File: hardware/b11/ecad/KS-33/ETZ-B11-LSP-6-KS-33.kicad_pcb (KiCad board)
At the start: 2 copper layers, 163.9 x 90.2 mm, 339 parts

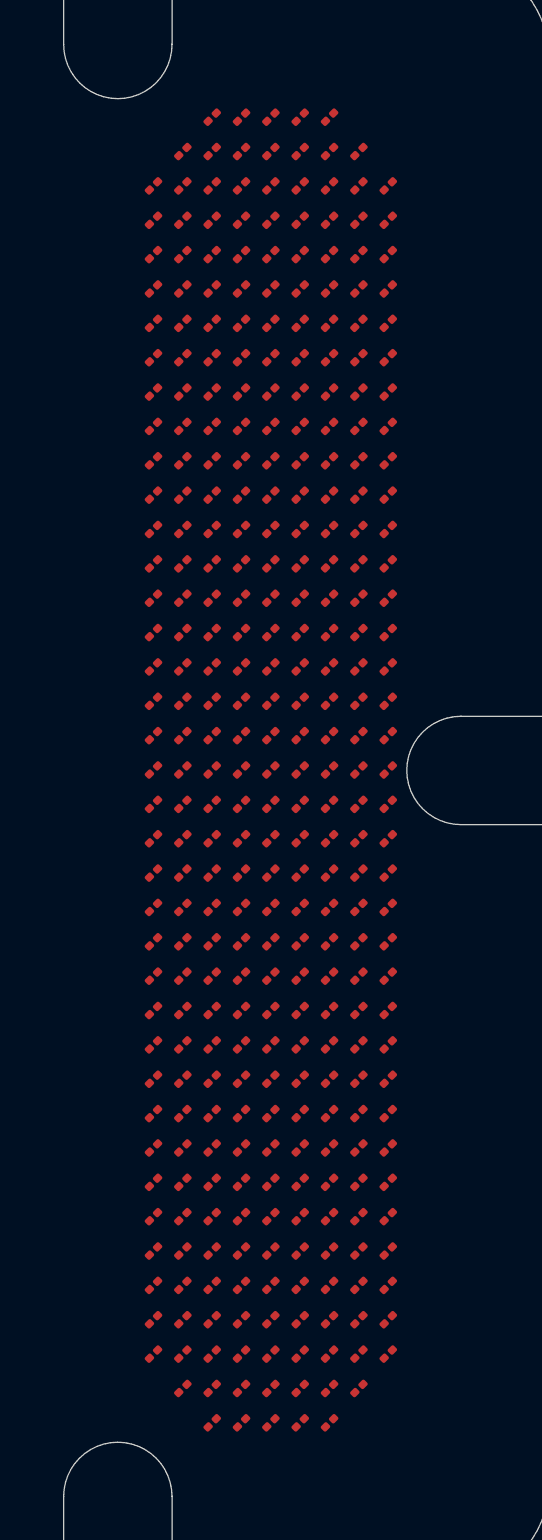
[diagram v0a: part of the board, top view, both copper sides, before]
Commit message: Adjust B11 display LED layout [skip ci]
Signed-off-by: Nikola Secerovski <secersh@gmail.com>
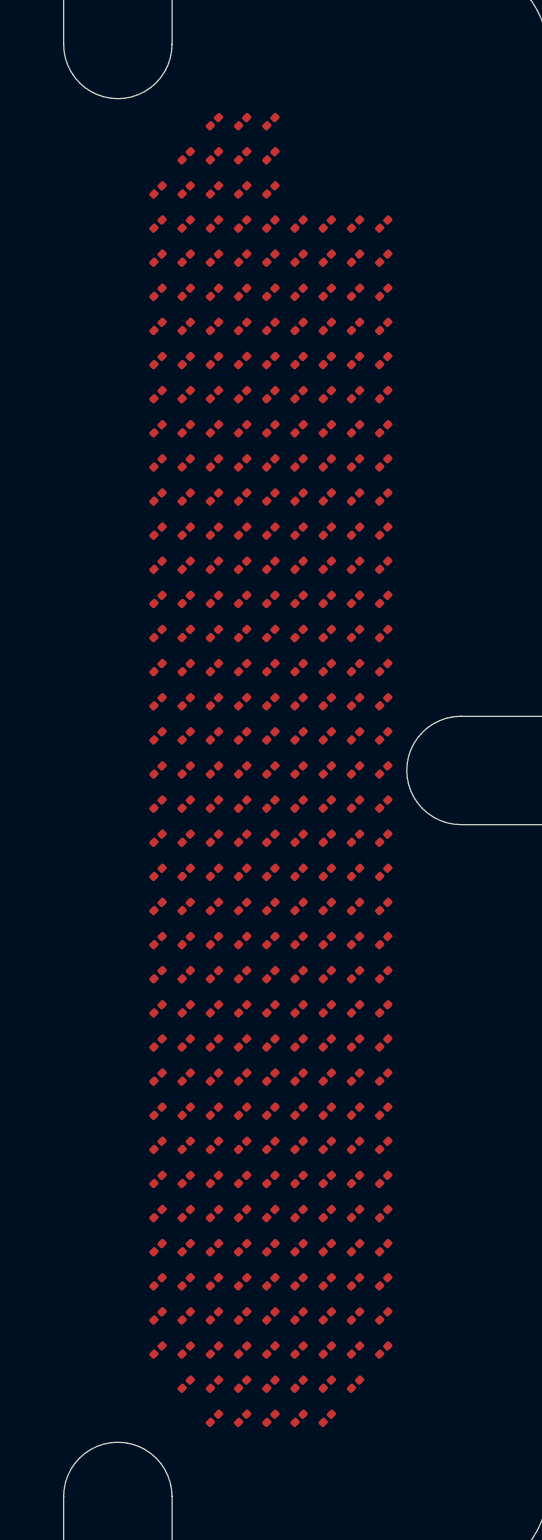
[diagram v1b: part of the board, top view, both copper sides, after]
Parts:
- removed D331, D332, D333, D334, D335, D336, D337, D338, D339: 0201_LED, 0201_LED
- moved D327 8.81 mm to (213.5, 140.2), turned to -135 degrees
- moved D326 8.75 mm to (211.9, 140.2), turned to -135 degrees
- moved D5 6.72 mm to (211.9, 70.3), turned to -135 degrees
- moved D4 6.67 mm to (210.3, 70.3), turned to -135 degrees
- moved D12 5.32 mm to (215.0, 72.2), turned to -135 degrees
- moved D11 5.26 mm to (213.5, 72.2), turned to -135 degrees
- moved D10 5.20 mm to (211.9, 72.2), turned to -135 degrees
- moved D328 5.15 mm to (215.0, 140.2), turned to -135 degrees
- moved D9 5.15 mm to (210.3, 72.2), turned to -135 degrees
- moved D8 5.09 mm to (208.8, 72.2), turned to -135 degrees
- moved D329 5.09 mm to (216.6, 140.2), turned to -135 degrees
- moved D330 5.03 mm to (218.2, 140.2), turned to -135 degrees
- moved D6 3.32 mm to (213.5, 70.3), turned to -135 degrees
- moved D7 3.26 mm to (215.0, 70.3), turned to -135 degrees
- moved D319 2.46 mm to (210.3, 138.3), turned to -135 degrees
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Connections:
- D10 pad 1: LED_CS2 -> LED_CS3
- D10 pad 2: LED_SW6 -> LED_SW3
- D100 pad 1: LED_CS12 -> LED_CS13
- D101 pad 1: LED_CS12 -> LED_CS13
- D102 pad 1: LED_CS12 -> LED_CS13
- D103 pad 1: LED_CS13 -> LED_CS14
- D104 pad 1: LED_CS13 -> LED_CS14
- D105 pad 1: LED_CS13 -> LED_CS14
- D106 pad 1: LED_CS13 -> LED_CS14
- D107 pad 1: LED_CS13 -> LED_CS14
- D108 pad 1: LED_CS13 -> LED_CS14
- D109 pad 1: LED_CS13 -> LED_CS14
- D11 pad 1: LED_CS2 -> LED_CS3
- D11 pad 2: LED_SW7 -> LED_SW4
- D110 pad 1: LED_CS13 -> LED_CS14
- D111 pad 1: LED_CS13 -> LED_CS14
- D112 pad 1: LED_CS14 -> LED_CS15
- D113 pad 1: LED_CS14 -> LED_CS15
- D114 pad 1: LED_CS14 -> LED_CS15
- D115 pad 1: LED_CS14 -> LED_CS15
- D116 pad 1: LED_CS14 -> LED_CS15
- D117 pad 1: LED_CS14 -> LED_CS15
- D118 pad 1: LED_CS14 -> LED_CS15
- D119 pad 1: LED_CS14 -> LED_CS15
- D12 pad 1: LED_CS2 -> LED_CS3
- D12 pad 2: LED_SW8 -> LED_SW5
- D120 pad 1: LED_CS14 -> LED_CS15
- D121 pad 1: LED_CS15 -> LED_CS16
- D122 pad 1: LED_CS15 -> LED_CS16
- D123 pad 1: LED_CS15 -> LED_CS16
- D124 pad 1: LED_CS15 -> LED_CS16
- D125 pad 1: LED_CS15 -> LED_CS16
- D126 pad 1: LED_CS15 -> LED_CS16
- D127 pad 1: LED_CS15 -> LED_CS16
- D128 pad 1: LED_CS15 -> LED_CS16
- D129 pad 1: LED_CS15 -> LED_CS16
- D13 pad 1: LED_CS3 -> LED_CS4
- D130 pad 1: LED_CS16 -> LED_CS17
- D131 pad 1: LED_CS16 -> LED_CS17
- D132 pad 1: LED_CS16 -> LED_CS17
- D133 pad 1: LED_CS16 -> LED_CS17
- D134 pad 1: LED_CS16 -> LED_CS17
- D135 pad 1: LED_CS16 -> LED_CS17
- D136 pad 1: LED_CS16 -> LED_CS17
- D137 pad 1: LED_CS16 -> LED_CS17
- D138 pad 1: LED_CS16 -> LED_CS17
- D139 pad 1: LED_CS17 -> LED_CS18
- D14 pad 1: LED_CS3 -> LED_CS4
- D140 pad 1: LED_CS17 -> LED_CS18
- D141 pad 1: LED_CS17 -> LED_CS18
- D142 pad 1: LED_CS17 -> LED_CS18
- D143 pad 1: LED_CS17 -> LED_CS18
- D144 pad 1: LED_CS17 -> LED_CS18
- D145 pad 1: LED_CS17 -> LED_CS18
- D146 pad 1: LED_CS17 -> LED_CS18
- D147 pad 1: LED_CS17 -> LED_CS18
- D148 pad 1: LED_CS18 -> LED_CS19
- D149 pad 1: LED_CS18 -> LED_CS19
- D15 pad 1: LED_CS3 -> LED_CS4
- D150 pad 1: LED_CS18 -> LED_CS19
- D151 pad 1: LED_CS18 -> LED_CS19
- D152 pad 1: LED_CS18 -> LED_CS19
- D153 pad 1: LED_CS18 -> LED_CS19
- D154 pad 1: LED_CS18 -> LED_CS19
- D155 pad 1: LED_CS18 -> LED_CS19
- D156 pad 1: LED_CS18 -> LED_CS19
- D157 pad 1: LED_CS19 -> LED_CS20
- D158 pad 1: LED_CS19 -> LED_CS20
- D159 pad 1: LED_CS19 -> LED_CS20
- D16 pad 1: LED_CS3 -> LED_CS4
- D160 pad 1: LED_CS19 -> LED_CS20
- D161 pad 1: LED_CS19 -> LED_CS20
- D162 pad 1: LED_CS19 -> LED_CS20
- D163 pad 1: LED_CS19 -> LED_CS20
- D164 pad 1: LED_CS19 -> LED_CS20
- D165 pad 1: LED_CS19 -> LED_CS20
- D166 pad 1: LED_CS20 -> LED_CS21
- D167 pad 1: LED_CS20 -> LED_CS21
- D168 pad 1: LED_CS20 -> LED_CS21
- D169 pad 1: LED_CS20 -> LED_CS21
- D17 pad 1: LED_CS3 -> LED_CS4
- D170 pad 1: LED_CS20 -> LED_CS21
- D171 pad 1: LED_CS20 -> LED_CS21
- D172 pad 1: LED_CS20 -> LED_CS21
- D173 pad 1: LED_CS20 -> LED_CS21
- D174 pad 1: LED_CS20 -> LED_CS21
- D175 pad 1: LED_CS21 -> LED_CS22
- D176 pad 1: LED_CS21 -> LED_CS22
- D177 pad 1: LED_CS21 -> LED_CS22
- D178 pad 1: LED_CS21 -> LED_CS22
- D179 pad 1: LED_CS21 -> LED_CS22
- D18 pad 1: LED_CS3 -> LED_CS4
- D180 pad 1: LED_CS21 -> LED_CS22
- D181 pad 1: LED_CS21 -> LED_CS22
- D182 pad 1: LED_CS21 -> LED_CS22
- D183 pad 1: LED_CS21 -> LED_CS22
- D184 pad 1: LED_CS22 -> LED_CS23
- D185 pad 1: LED_CS22 -> LED_CS23
- D186 pad 1: LED_CS22 -> LED_CS23
- D187 pad 1: LED_CS22 -> LED_CS23
- D188 pad 1: LED_CS22 -> LED_CS23
- D189 pad 1: LED_CS22 -> LED_CS23
- D19 pad 1: LED_CS3 -> LED_CS4
- D190 pad 1: LED_CS22 -> LED_CS23
- D191 pad 1: LED_CS22 -> LED_CS23
- D192 pad 1: LED_CS22 -> LED_CS23
- D193 pad 1: LED_CS23 -> LED_CS24
- D194 pad 1: LED_CS23 -> LED_CS24
- D195 pad 1: LED_CS23 -> LED_CS24
- D196 pad 1: LED_CS23 -> LED_CS24
- D197 pad 1: LED_CS23 -> LED_CS24
- D198 pad 1: LED_CS23 -> LED_CS24
- D199 pad 1: LED_CS23 -> LED_CS24
- D20 pad 1: LED_CS3 -> LED_CS4
- D200 pad 1: LED_CS23 -> LED_CS24
- D201 pad 1: LED_CS23 -> LED_CS24
- D202 pad 1: LED_CS24 -> LED_CS25
- D203 pad 1: LED_CS24 -> LED_CS25
- D204 pad 1: LED_CS24 -> LED_CS25
- D205 pad 1: LED_CS24 -> LED_CS25
- D206 pad 1: LED_CS24 -> LED_CS25
- D207 pad 1: LED_CS24 -> LED_CS25
- D208 pad 1: LED_CS24 -> LED_CS25
- D209 pad 1: LED_CS24 -> LED_CS25
- D21 pad 1: LED_CS3 -> LED_CS4
- D210 pad 1: LED_CS24 -> LED_CS25
- D211 pad 1: LED_CS25 -> LED_CS26
- D212 pad 1: LED_CS25 -> LED_CS26
- D213 pad 1: LED_CS25 -> LED_CS26
- D214 pad 1: LED_CS25 -> LED_CS26
- D215 pad 1: LED_CS25 -> LED_CS26
- D216 pad 1: LED_CS25 -> LED_CS26
- D217 pad 1: LED_CS25 -> LED_CS26
- D218 pad 1: LED_CS25 -> LED_CS26
- D219 pad 1: LED_CS25 -> LED_CS26
- D22 pad 1: LED_CS4 -> LED_CS5
- D220 pad 1: LED_CS26 -> LED_CS27
- D221 pad 1: LED_CS26 -> LED_CS27
- D222 pad 1: LED_CS26 -> LED_CS27
- D223 pad 1: LED_CS26 -> LED_CS27
- D224 pad 1: LED_CS26 -> LED_CS27
- D225 pad 1: LED_CS26 -> LED_CS27
- D226 pad 1: LED_CS26 -> LED_CS27
- D227 pad 1: LED_CS26 -> LED_CS27
- D228 pad 1: LED_CS26 -> LED_CS27
- D229 pad 1: LED_CS27 -> LED_CS28
- D23 pad 1: LED_CS4 -> LED_CS5
- D230 pad 1: LED_CS27 -> LED_CS28
- D231 pad 1: LED_CS27 -> LED_CS28
- D232 pad 1: LED_CS27 -> LED_CS28
- D233 pad 1: LED_CS27 -> LED_CS28
- D234 pad 1: LED_CS27 -> LED_CS28
- D235 pad 1: LED_CS27 -> LED_CS28
- D236 pad 1: LED_CS27 -> LED_CS28
- D237 pad 1: LED_CS27 -> LED_CS28
- D238 pad 1: LED_CS28 -> LED_CS29
- D239 pad 1: LED_CS28 -> LED_CS29
- D24 pad 1: LED_CS4 -> LED_CS5
- D240 pad 1: LED_CS28 -> LED_CS29
- D241 pad 1: LED_CS28 -> LED_CS29
- D242 pad 1: LED_CS28 -> LED_CS29
- D243 pad 1: LED_CS28 -> LED_CS29
- D244 pad 1: LED_CS28 -> LED_CS29
- D245 pad 1: LED_CS28 -> LED_CS29
- D246 pad 1: LED_CS28 -> LED_CS29
- D247 pad 1: LED_CS29 -> LED_CS30
- D248 pad 1: LED_CS29 -> LED_CS30
- D249 pad 1: LED_CS29 -> LED_CS30
- D25 pad 1: LED_CS4 -> LED_CS5
- D250 pad 1: LED_CS29 -> LED_CS30
- D251 pad 1: LED_CS29 -> LED_CS30
- D252 pad 1: LED_CS29 -> LED_CS30
- D253 pad 1: LED_CS29 -> LED_CS30
- D254 pad 1: LED_CS29 -> LED_CS30
- D255 pad 1: LED_CS29 -> LED_CS30
- D256 pad 1: LED_CS30 -> LED_CS31
- D257 pad 1: LED_CS30 -> LED_CS31
- D258 pad 1: LED_CS30 -> LED_CS31
- D259 pad 1: LED_CS30 -> LED_CS31
- D26 pad 1: LED_CS4 -> LED_CS5
- D260 pad 1: LED_CS30 -> LED_CS31
- D261 pad 1: LED_CS30 -> LED_CS31
- D262 pad 1: LED_CS30 -> LED_CS31
- D263 pad 1: LED_CS30 -> LED_CS31
- D264 pad 1: LED_CS30 -> LED_CS31
- D265 pad 1: LED_CS31 -> LED_CS32
- D266 pad 1: LED_CS31 -> LED_CS32
- D267 pad 1: LED_CS31 -> LED_CS32
- D268 pad 1: LED_CS31 -> LED_CS32
- D269 pad 1: LED_CS31 -> LED_CS32
- D27 pad 1: LED_CS4 -> LED_CS5
- D270 pad 1: LED_CS31 -> LED_CS32
- D271 pad 1: LED_CS31 -> LED_CS32
- D272 pad 1: LED_CS31 -> LED_CS32
- D273 pad 1: LED_CS31 -> LED_CS32
- D274 pad 1: LED_CS32 -> LED_CS33
- D275 pad 1: LED_CS32 -> LED_CS33
- D276 pad 1: LED_CS32 -> LED_CS33
- D277 pad 1: LED_CS32 -> LED_CS33
- D278 pad 1: LED_CS32 -> LED_CS33
- D279 pad 1: LED_CS32 -> LED_CS33
- D28 pad 1: LED_CS4 -> LED_CS5
- D280 pad 1: LED_CS32 -> LED_CS33
- D281 pad 1: LED_CS32 -> LED_CS33
- D282 pad 1: LED_CS32 -> LED_CS33
- D283 pad 1: LED_CS33 -> LED_CS34
- D284 pad 1: LED_CS33 -> LED_CS34
- D285 pad 1: LED_CS33 -> LED_CS34
- D286 pad 1: LED_CS33 -> LED_CS34
- D287 pad 1: LED_CS33 -> LED_CS34
- D288 pad 1: LED_CS33 -> LED_CS34
- D289 pad 1: LED_CS33 -> LED_CS34
- D29 pad 1: LED_CS4 -> LED_CS5
- D290 pad 1: LED_CS33 -> LED_CS34
- D291 pad 1: LED_CS33 -> LED_CS34
- D292 pad 1: LED_CS34 -> LED_CS35
- D293 pad 1: LED_CS34 -> LED_CS35
- D294 pad 1: LED_CS34 -> LED_CS35
- D295 pad 1: LED_CS34 -> LED_CS35
- D296 pad 1: LED_CS34 -> LED_CS35
- D297 pad 1: LED_CS34 -> LED_CS35
- D298 pad 1: LED_CS34 -> LED_CS35
- D299 pad 1: LED_CS34 -> LED_CS35
- D30 pad 1: LED_CS4 -> LED_CS5
- D300 pad 1: LED_CS34 -> LED_CS35
- D301 pad 1: LED_CS35 -> LED_CS36
- D302 pad 1: LED_CS35 -> LED_CS36
- D303 pad 1: LED_CS35 -> LED_CS36
- D304 pad 1: LED_CS35 -> LED_CS36
- D305 pad 1: LED_CS35 -> LED_CS36
- D306 pad 1: LED_CS35 -> LED_CS36
- D307 pad 1: LED_CS35 -> LED_CS36
- D308 pad 1: LED_CS35 -> LED_CS36
- D309 pad 1: LED_CS35 -> LED_CS36
- D31 pad 1: LED_CS5 -> LED_CS6
- D310 pad 1: LED_CS36 -> LED_CS37
- D311 pad 1: LED_CS36 -> LED_CS37
- D312 pad 1: LED_CS36 -> LED_CS37
- D313 pad 1: LED_CS36 -> LED_CS37
- D314 pad 1: LED_CS36 -> LED_CS37
- D315 pad 1: LED_CS36 -> LED_CS37
- D316 pad 1: LED_CS36 -> LED_CS37
- D317 pad 1: LED_CS36 -> LED_CS37
- D318 pad 1: LED_CS36 -> LED_CS37
- D319 pad 1: LED_CS37 -> LED_CS38
- D319 pad 2: LED_SW1 -> LED_SW2
- D32 pad 1: LED_CS5 -> LED_CS6
- D320 pad 1: LED_CS37 -> LED_CS38
- D320 pad 2: LED_SW2 -> LED_SW3
- D321 pad 1: LED_CS37 -> LED_CS38
- D321 pad 2: LED_SW3 -> LED_SW4
- D322 pad 1: LED_CS37 -> LED_CS38
- D322 pad 2: LED_SW4 -> LED_SW5
- D323 pad 1: LED_CS37 -> LED_CS38
- D323 pad 2: LED_SW5 -> LED_SW6
- D324 pad 1: LED_CS37 -> LED_CS38
- D324 pad 2: LED_SW6 -> LED_SW7
- D325 pad 1: LED_CS37 -> LED_CS38
- D325 pad 2: LED_SW7 -> LED_SW8
- D326 pad 1: LED_CS37 -> LED_CS39
- D326 pad 2: LED_SW8 -> LED_SW3
- D327 pad 1: LED_CS37 -> LED_CS39
- D327 pad 2: LED_SW9 -> LED_SW4
- D328 pad 1: LED_CS38 -> LED_CS39
- D328 pad 2: LED_SW2 -> LED_SW5
- D329 pad 1: LED_CS38 -> LED_CS39
- D329 pad 2: LED_SW3 -> LED_SW6
- D33 pad 1: LED_CS5 -> LED_CS6
- D330 pad 1: LED_CS38 -> LED_CS39
- D330 pad 2: LED_SW4 -> LED_SW7
- D34 pad 1: LED_CS5 -> LED_CS6
- D35 pad 1: LED_CS5 -> LED_CS6
- D36 pad 1: LED_CS5 -> LED_CS6
- D37 pad 1: LED_CS5 -> LED_CS6
- D38 pad 1: LED_CS5 -> LED_CS6
- D39 pad 1: LED_CS5 -> LED_CS6
- D4 pad 1: LED_CS1 -> LED_CS2
- D4 pad 2: LED_SW6 -> LED_SW2
- D40 pad 1: LED_CS6 -> LED_CS7
- D41 pad 1: LED_CS6 -> LED_CS7
- D42 pad 1: LED_CS6 -> LED_CS7
- D43 pad 1: LED_CS6 -> LED_CS7
- D44 pad 1: LED_CS6 -> LED_CS7
- D45 pad 1: LED_CS6 -> LED_CS7
- D46 pad 1: LED_CS6 -> LED_CS7
- D47 pad 1: LED_CS6 -> LED_CS7
- D48 pad 1: LED_CS6 -> LED_CS7
- D49 pad 1: LED_CS7 -> LED_CS8
- D5 pad 1: LED_CS1 -> LED_CS2
- D5 pad 2: LED_SW7 -> LED_SW3
- D50 pad 1: LED_CS7 -> LED_CS8
- D51 pad 1: LED_CS7 -> LED_CS8
- D52 pad 1: LED_CS7 -> LED_CS8
- D53 pad 1: LED_CS7 -> LED_CS8
- D54 pad 1: LED_CS7 -> LED_CS8
- D55 pad 1: LED_CS7 -> LED_CS8
- D56 pad 1: LED_CS7 -> LED_CS8
- D57 pad 1: LED_CS7 -> LED_CS8
- D58 pad 1: LED_CS8 -> LED_CS9
- D59 pad 1: LED_CS8 -> LED_CS9
- D6 pad 2: LED_SW2 -> LED_SW4
- D60 pad 1: LED_CS8 -> LED_CS9
- D61 pad 1: LED_CS8 -> LED_CS9
- D62 pad 1: LED_CS8 -> LED_CS9
- D63 pad 1: LED_CS8 -> LED_CS9
- D64 pad 1: LED_CS8 -> LED_CS9
- D65 pad 1: LED_CS8 -> LED_CS9
- D66 pad 1: LED_CS8 -> LED_CS9
- D67 pad 1: LED_CS9 -> LED_CS10
- D68 pad 1: LED_CS9 -> LED_CS10
- D69 pad 1: LED_CS9 -> LED_CS10
- D7 pad 2: LED_SW3 -> LED_SW5
- D70 pad 1: LED_CS9 -> LED_CS10
- D71 pad 1: LED_CS9 -> LED_CS10
- D72 pad 1: LED_CS9 -> LED_CS10
- D73 pad 1: LED_CS9 -> LED_CS10
- D74 pad 1: LED_CS9 -> LED_CS10
- D75 pad 1: LED_CS9 -> LED_CS10
- D76 pad 1: LED_CS10 -> LED_CS11
- D77 pad 1: LED_CS10 -> LED_CS11
- D78 pad 1: LED_CS10 -> LED_CS11
- D79 pad 1: LED_CS10 -> LED_CS11
- D8 pad 1: LED_CS2 -> LED_CS3
- D8 pad 2: LED_SW4 -> LED_SW1
- D80 pad 1: LED_CS10 -> LED_CS11
- D81 pad 1: LED_CS10 -> LED_CS11
- D82 pad 1: LED_CS10 -> LED_CS11
- D83 pad 1: LED_CS10 -> LED_CS11
- D84 pad 1: LED_CS10 -> LED_CS11
- D85 pad 1: LED_CS11 -> LED_CS12
- D86 pad 1: LED_CS11 -> LED_CS12
- D87 pad 1: LED_CS11 -> LED_CS12
- D88 pad 1: LED_CS11 -> LED_CS12
- D89 pad 1: LED_CS11 -> LED_CS12
- D9 pad 1: LED_CS2 -> LED_CS3
- D9 pad 2: LED_SW5 -> LED_SW2
- D90 pad 1: LED_CS11 -> LED_CS12
- D91 pad 1: LED_CS11 -> LED_CS12
- D92 pad 1: LED_CS11 -> LED_CS12
- D93 pad 1: LED_CS11 -> LED_CS12
- D94 pad 1: LED_CS12 -> LED_CS13
- D95 pad 1: LED_CS12 -> LED_CS13
- D96 pad 1: LED_CS12 -> LED_CS13
- D97 pad 1: LED_CS12 -> LED_CS13
- D98 pad 1: LED_CS12 -> LED_CS13
- D99 pad 1: LED_CS12 -> LED_CS13

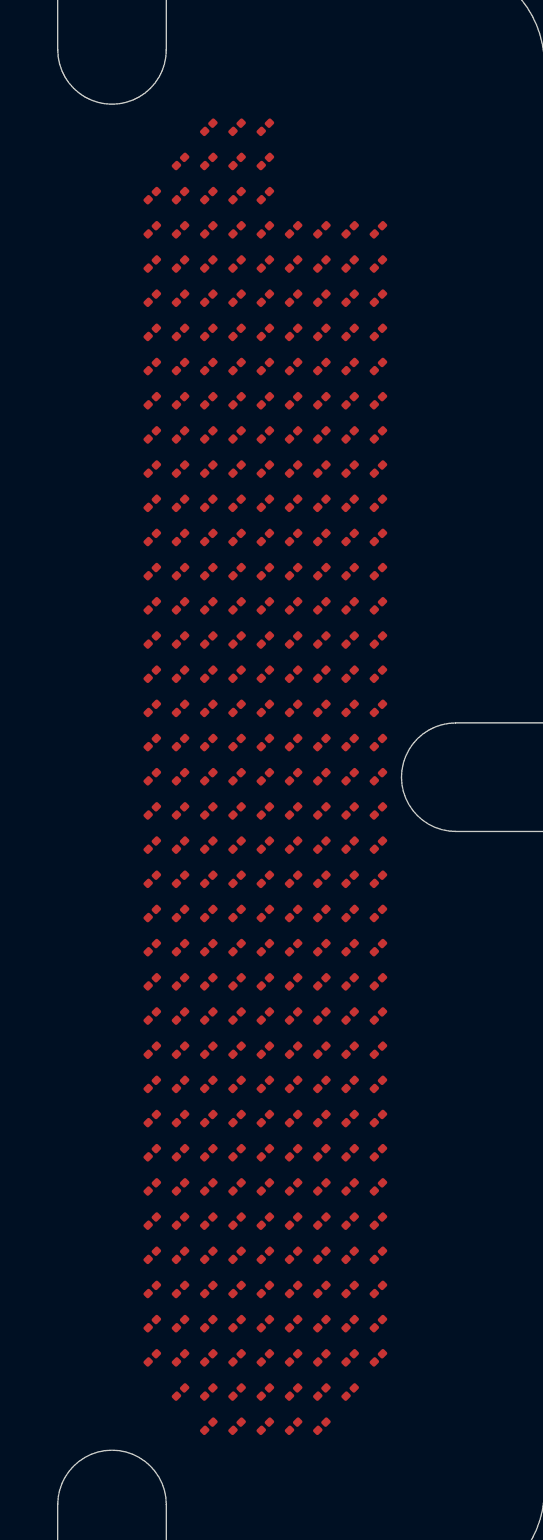
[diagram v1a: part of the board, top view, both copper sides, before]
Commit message: Route B11 display LED matrix [skip ci]
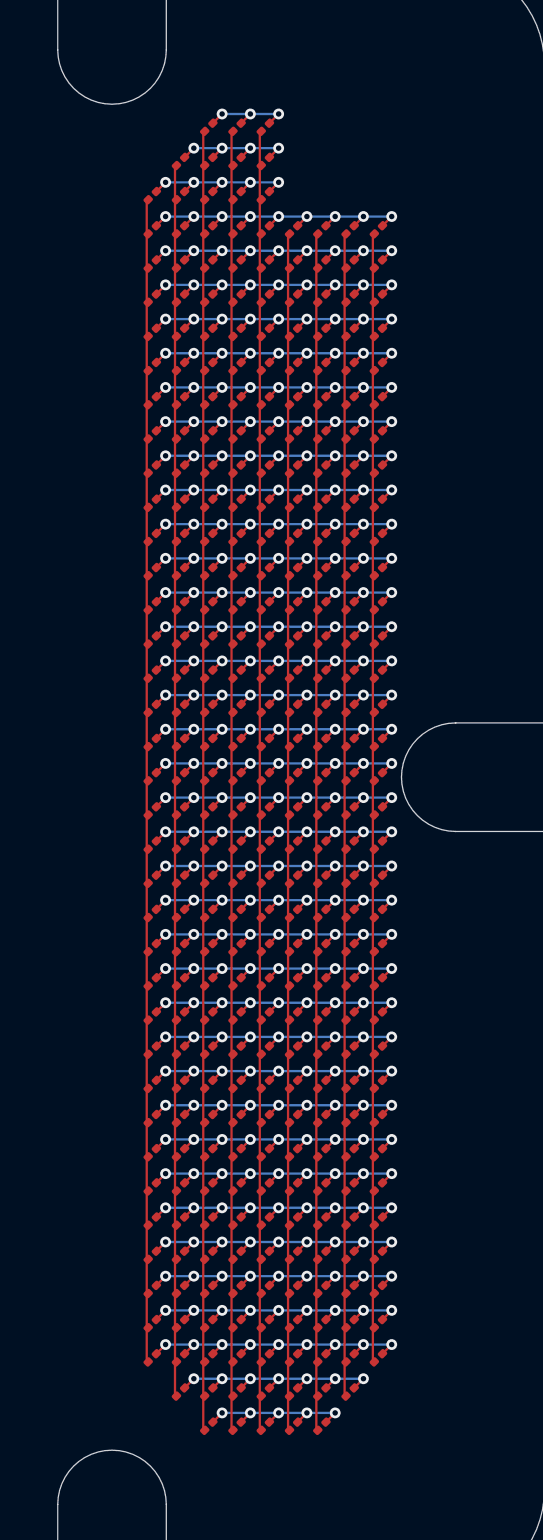
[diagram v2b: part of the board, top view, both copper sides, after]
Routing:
- net LED_SW5: track 0.00 -> 74.9 mm
- net LED_SW4: track 0.00 -> 74.9 mm
- net LED_SW3: track 0.00 -> 74.9 mm
- net LED_SW2: track 0.00 -> 71.0 mm
- net LED_SW7: track 0.00 -> 69.0 mm
- net LED_SW6: track 0.00 -> 69.0 mm
- net LED_SW8: track 0.00 -> 67.0 mm
- net LED_SW1: track 0.00 -> 67.0 mm
- net LED_SW9: track 0.00 -> 65.1 mm
- net LED_CS9: track 0.00 -> 19.0 mm, vias 0 -> 9
- net LED_CS7: track 0.00 -> 19.0 mm, vias 0 -> 9
- net LED_CS5: track 0.00 -> 19.0 mm, vias 0 -> 9
- net LED_CS4: track 0.00 -> 19.0 mm, vias 0 -> 9
- net LED_CS37: track 0.00 -> 19.0 mm, vias 0 -> 9
- net LED_CS36: track 0.00 -> 19.0 mm, vias 0 -> 9
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
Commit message: Prototype B11 display driver fanout [skip ci]
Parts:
- removed D1, D10, D100, D101, D102, D103, D104, D105, D106, D107, D108, D109, D11, D110, D111, D112, D113, D114, D115, D116, D117, D118, D119, D12, D120, D121, D122, D123, D124, D125, D126, D127, D128, D129, D13, D130, D131, D132, D133, D134, D135, D136, D137, D138, D139, D14, D140, D141, D142, D143, D144, D145, D146, D147, D148, D149, D15, D150, D151, D152, D153, D154, D155, D156, D157, D158, D159, D16, D160, D161, D162, D163, D164, D165, D166, D167, D168, D169, D17, D170, D171, D172, D173, D174, D175, D176, D177, D178, D179, D18, D180, D181, D182, D183, D184, D185, D186, D187, D188, D189, D19, D190, D191, D192, D193, D194, D195, D196, D197, D198, D199, D2, D20, D200, D201, D202, D203, D204, D205, D206, D207, D208, D209, D21, D210, D211, D212, D213, D214, D215, D216, D217, D218, D219, D22, D220, D221, D222, D223, D224, D225, D226, D227, D228, D229, D23, D230, D231, D232, D233, D234, D235, D236, D237, D238, D239, D24, D240, D241, D242, D243, D244, D245, D246, D247, D248, D249, D25, D250, D251, D252, D253, D254, D255, D256, D257, D258, D259, D26, D260, D261, D262, D263, D264, D265, D266, D267, D268, D269, D27, D270, D271, D272, D273, D274, D275, D276, D277, D278, D279, D28, D280, D281, D282, D283, D284, D285, D286, D287, D288, D289, D29, D290, D291, D292, D293, D294, D295, D296, D297, D298, D299, D3, D30, D300, D301, D302, D303, D304, D305, D306, D307, D308, D309, D31, D310, D311, D312, D313, D314, D315, D316, D317, D318, D319, D32, D320, D321, D322, D323, D324, D325, D326, D327, D328, D329, D33, D330, D34, D35, D36, D37, D38, D39, D4, D40, D41, D42, D43, D44, D45, D46, D47, D48, D49, D5, D50, D51, D52, D53, D54, D55, D56, D57, D58, D59, D6, D60, D61, D62, D63, D64, D65, D66, D67, D68, D69, D7, D70, D71, D72, D73, D74, D75, D76, D77, D78, D79, D8, D80, D81, D82, D83, D84, D85, D86, D87, D88, D89, D9, D90, D91, D92, D93, D94, D95, D96, D97, D98, D99: 0201_LED, 0201_LED
- added J_DSP1: ETZ-B11-DSP-EDGE-48, ETZ-B11-DSP-EDGE-48, B.Cu at (208.2, 73.8)
- added U_DSP1: IS31FL3741A, IS31FL3741A-QFN-60-7x7, B.Cu at (215.2, 104.4)
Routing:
- net LED_SW8: track 67.0 -> 0.00 mm
- net LED_SW9: track 65.1 -> 0.00 mm
- net LED_SW3: track 74.9 -> 17.2 mm
- net LED_SW4: track 74.9 -> 18.6 mm
- net LED_SW2: track 71.0 -> 15.8 mm
- net LED_SW5: track 74.9 -> 20.1 mm
- net LED_SW1: track 67.0 -> 14.6 mm
- net LED_SW6: track 69.0 -> 21.5 mm
- net LED_SW7: track 69.0 -> 22.9 mm
- net LED_CS1: track 5.28 -> 27.6 mm, vias 3 -> 0
- net LED_CS9: track 19.0 -> 0.00 mm, vias 9 -> 0
- net LED_CS7: track 19.0 -> 0.00 mm, vias 9 -> 0
- net LED_CS14: track 19.0 -> 0.00 mm, vias 9 -> 0
- net LED_CS13: track 19.0 -> 0.00 mm, vias 9 -> 0
- net LED_CS11: track 19.0 -> 0.00 mm, vias 9 -> 0
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
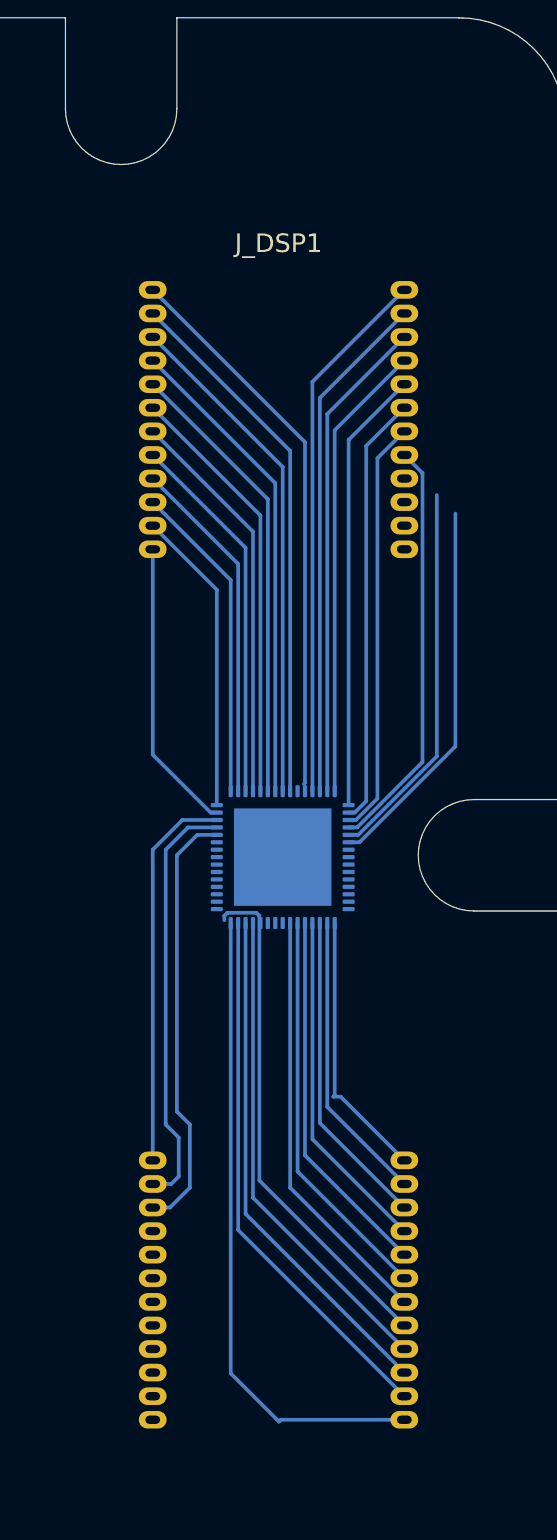
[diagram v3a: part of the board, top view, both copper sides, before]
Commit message: feat: add B11 display module attach footprint [skip ci]
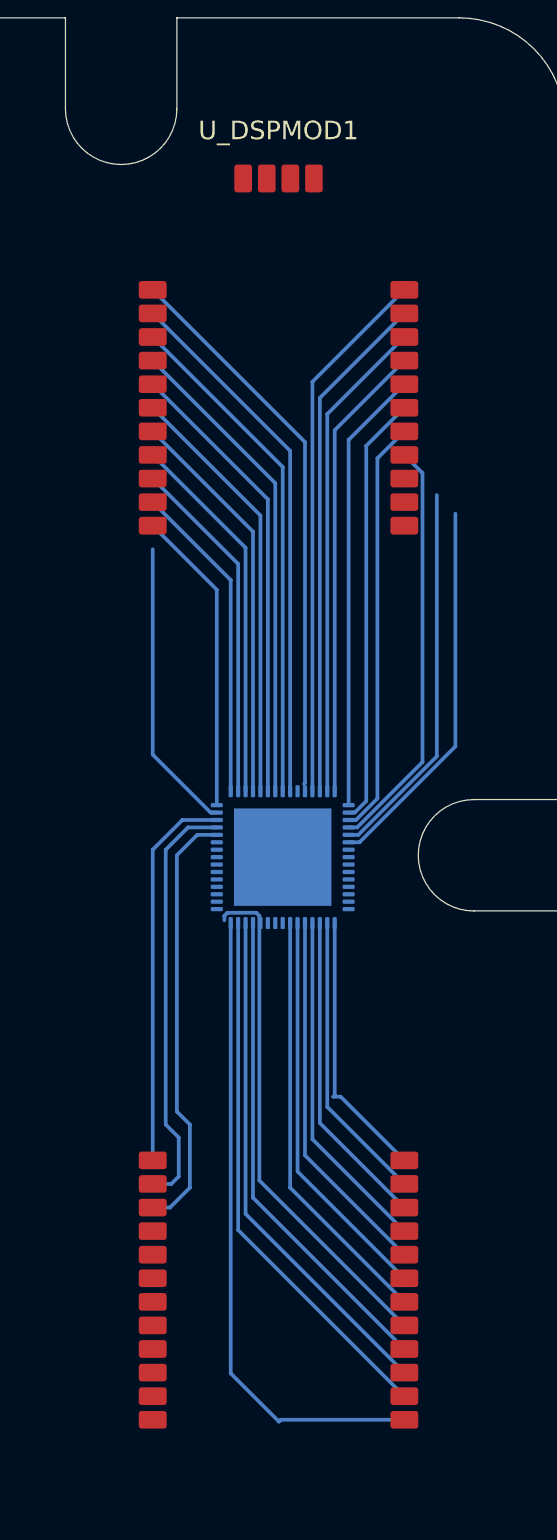
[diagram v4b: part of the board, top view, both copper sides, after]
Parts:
- removed J_DSP1: ETZ-B11-DSP-EDGE-48, ETZ-B11-DSP-EDGE-48
- added U_DSPMOD1: ETZ-B11-DSP, ETZ-B11-DSP, F.Cu at (215.0, 104.3)

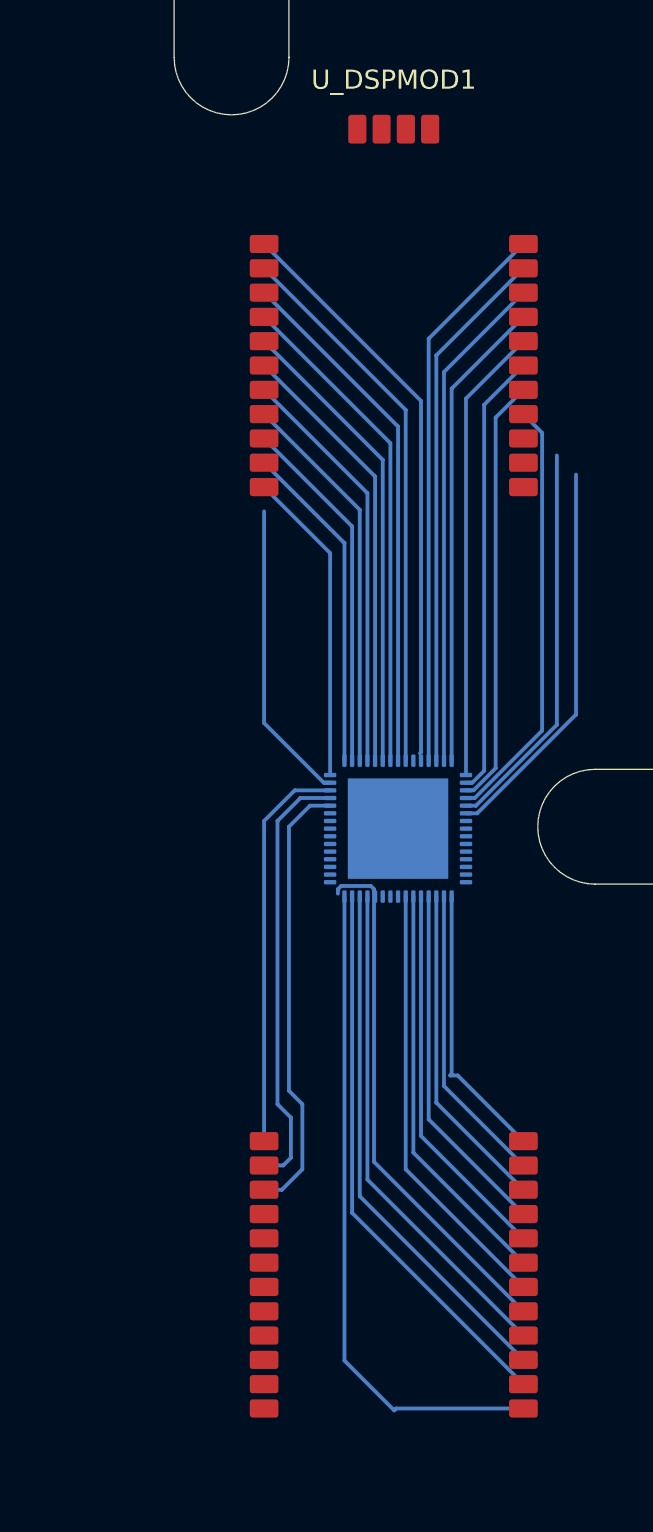
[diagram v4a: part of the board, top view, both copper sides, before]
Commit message: feat: add B11 LRA test footprint [skip ci]
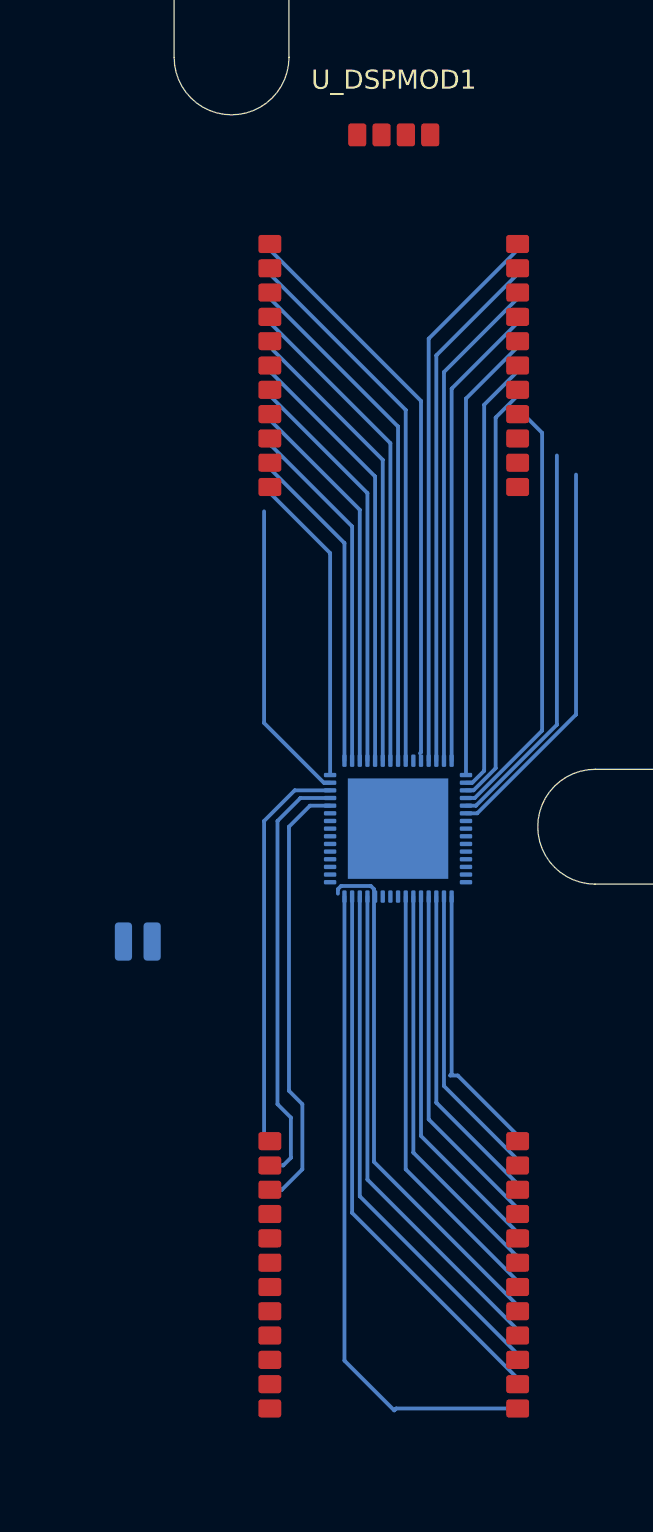
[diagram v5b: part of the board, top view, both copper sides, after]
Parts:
- added M_LRA1: VLV041235L-L20, VLV041235L-L20, B.Cu at (201.6, 102.3)
